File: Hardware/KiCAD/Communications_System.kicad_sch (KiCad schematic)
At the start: 1 part, among them IC2 CC1200RHBR

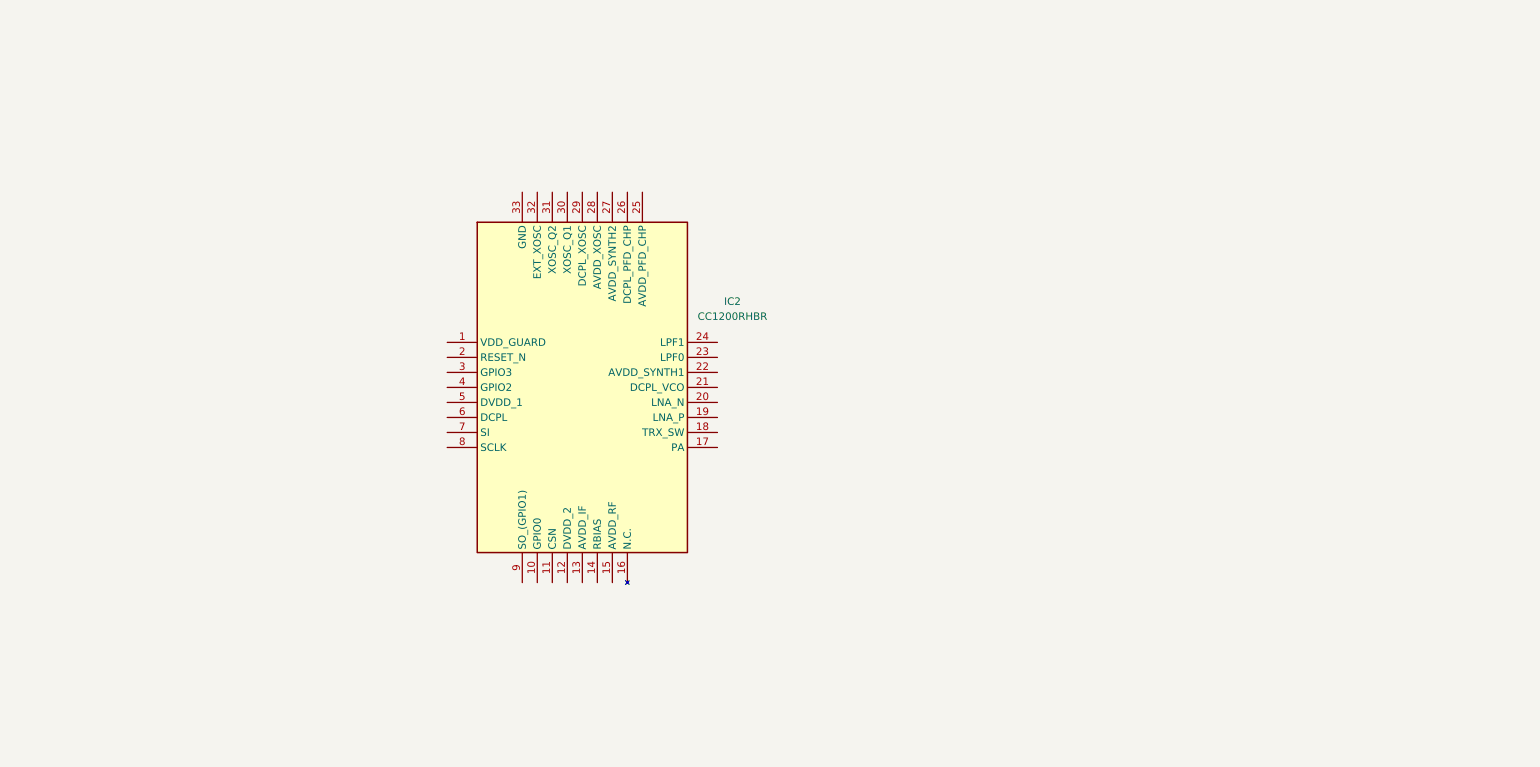
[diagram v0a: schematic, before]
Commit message: feat: Connect ESP32 to CC1200
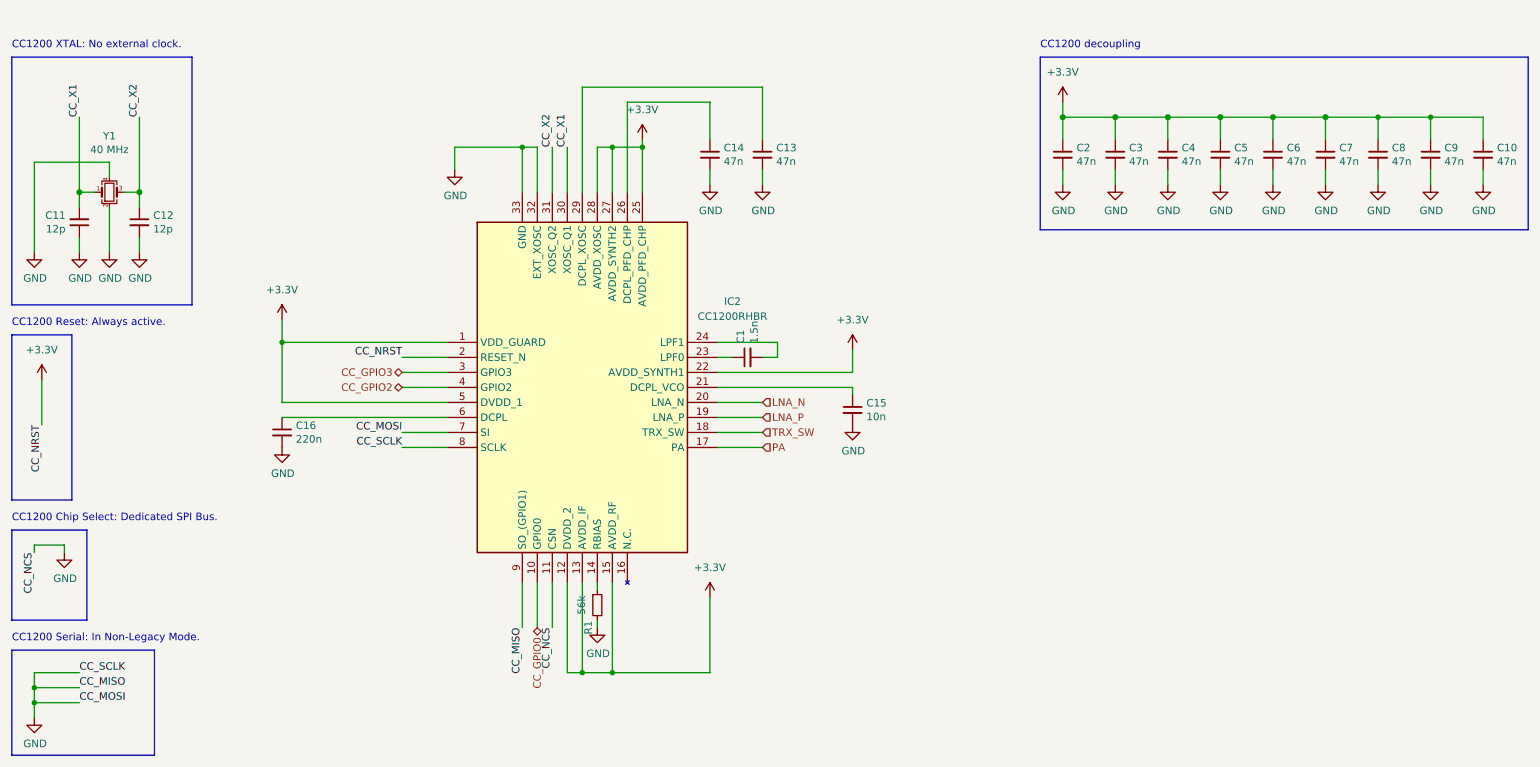
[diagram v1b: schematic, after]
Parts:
- added C1: 1.5n, Capacitor_SMD:C_0402_1005Metric, symbol pkl_device:pkl_C_Small
- added C10, C13, C14, C2, C3, C4, C5, C6, C7, C8, C9: 47n, Capacitor_SMD:C_0402_1005Metric, symbol pkl_device:pkl_C_Small
- added C11, C12: 12p, Capacitor_SMD:C_0402_1005Metric, symbol pkl_device:pkl_C_Small
- added C15: 10n, Capacitor_SMD:C_0402_1005Metric, symbol pkl_device:pkl_C_Small
- added C16: 220n, Capacitor_SMD:C_0402_1005Metric, symbol pkl_device:pkl_C_Small
- added R1: 56k, Resistor_SMD:R_0402_1005Metric, symbol pkl_device:pkl_R_Small
- added Y1: 40 MHz, Crystal:Crystal_SMD_3225-4Pin_3.2x2.5mm, symbol Device:Crystal_GND24_Small
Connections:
- net +3.3V: now reaches IC2.1 (VDD_GUARD)
- net +3.3V: now also IC2.12 (DVDD_2), IC2.13 (AVDD_IF), IC2.15 (AVDD_RF), IC2.2 (RESET_N), IC2.22 (AVDD_SYNTH1), IC2.25 (AVDD_PFD_CHP), IC2.27 (AVDD_SYNTH2), IC2.28 (AVDD_XOSC), IC2.5 (DVDD_1), C10.1, C2.1, C3.1, C4.1, C5.1, C6.1, C7.1, C8.1, C9.1
- net CC_GPIO0: now reaches IC2.10 (GPIO0)
- net GND: now reaches IC2.11 (CSN)
- net GND: now also IC2.32 (EXT_XOSC), IC2.33 (GND), IC2.7 (SI), IC2.8 (SCLK), IC2.9 (SO_(GPIO1)), C10.2, C11.1, C12.2, C13.2, C14.2, C15.2, C16.2, C2.2, C3.2, C4.2, C5.2, C6.2, C7.2, C8.2, C9.2, R1.2, Y1.2, Y1.4
- net at IC2.14 (RBIAS): now also R1.1
- net PA: now reaches IC2.17 (PA)
- net TRX_SW: now reaches IC2.18 (TRX_SW)
- net LNA_P: now reaches IC2.19 (LNA_P)
- net LNA_N: now reaches IC2.20 (LNA_N)
- net at IC2.21 (DCPL_VCO): now also C15.1
- net at IC2.23 (LPF0): now also C1.1
- net at IC2.24 (LPF1): now also C1.2
- net at IC2.26 (DCPL_PFD_CHP): now also C14.1
- net at IC2.29 (DCPL_XOSC): now also C13.1
- net CC_GPIO3: now reaches IC2.3 (GPIO3)
- net CC_X1: now reaches IC2.30 (XOSC_Q1)
- net CC_X1: now also C11.2, Y1.1
- net CC_X2: now reaches IC2.31 (XOSC_Q2)
- net CC_X2: now also C12.1, Y1.3
- net CC_GPIO2: now reaches IC2.4 (GPIO2)
- net at IC2.6 (DCPL): now also C16.1
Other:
- note added: "CC1200 Chip Select: Dedicated SPI Bus."
- note added: "CC1200 Reset: Always active."
- note added: "CC1200 Serial: In Non-Legacy Mode."
- note added: "CC1200 XTAL: No external clock."
- note added: "CC1200 decoupling"
- title: (none) -> RF Communications System

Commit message: feat: add models, correct hierarchical patterns
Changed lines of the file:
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@@
     (effects (font (size 1.27 1.27)) (justify left bottom))
-  )
-  (label "CC_MOSI" (at 85.09 83.82 180) (fields_autoplaced)
-    (effects (font (size 1.27 1.27)) (justify right bottom))
   )
   (label "CC_X1" (at 113.03 35.56 90) (fields_autoplaced)
@@
     (effects (font (size 1.27 1.27)) (justify left bottom))
   )
-  (label "CC_MISO" (at 105.41 116.84 270) (fields_autoplaced)
-    (effects (font (size 1.27 1.27)) (justify right bottom))
+  (label "CC_X2" (at 219.71 73.66 90) (fields_autoplaced)
+    (effects (font (size 1.27 1.27)) (justify left bottom))
   )
   (label "CC_NCS" (at 22.86 104.14 270) (fields_autoplaced)
     (effects (font (size 1.27 1.27)) (justify right bottom))
   )
+  (label "CC_X1" (at 209.55 73.66 90) (fields_autoplaced)
+    (effects (font (size 1.27 1.27)) (justify left bottom))
+  )
   (label "CC_X2" (at 110.49 35.56 90) (fields_autoplaced)
     (effects (font (size 1.27 1.27)) (justify left bottom))
   )
-  (label "CC_SCLK" (at 85.09 86.36 180) (fields_autoplaced)
-    (effects (font (size 1.27 1.27)) (justify right bottom))
-  )
-  (label "CC_NCS" (at 110.49 116.84 270) (fields_autoplaced)
-    (effects (font (size 1.27 1.27)) (justify right bottom))
-  )
   (label "CC_NRST" (at 24.13 82.55 270) (fields_autoplaced)
     (effects (font (size 1.27 1.27)) (justify right bottom))
@@
     (effects (font (size 1.27 1.27)) (justify left bottom))
   )
+  (hierarchical_label "CC_NCS" (shape input) (at 110.49 116.84 270) (fields_autoplaced)
+    (effects (font (size 1.27 1.27)) (justify right))
+  )
   (hierarchical_label "CC_GPIO3" (shape bidirectional) (at 85.09 73.66 180) (fields_autoplaced)
     (effects (font (size 1.27 1.27)) (justify right))
@@
     (effects (font (size 1.27 1.27)) (justify left))
   )
+  (hierarchical_label "CC_MISO" (shape output) (at 105.41 116.84 270) (fields_autoplaced)
+    (effects (font (size 1.27 1.27)) (justify right))
+  )
   (hierarchical_label "LNA_P" (shape input) (at 146.05 81.28 0) (fields_autoplaced)
     (effects (font (size 1.27 1.27)) (justify left))
   )
+  (hierarchical_label "CC_MOSI" (shape input) (at 85.09 83.82 180) (fields_autoplaced)
+    (effects (font (size 1.27 1.27)) (justify right))
+  )
   (hierarchical_label "PA" (shape input) (at 146.05 86.36 0) (fields_autoplaced)
     (effects (font (size 1.27 1.27)) (justify left))
@@
   (hierarchical_label "LNA_N" (shape input) (at 146.05 78.74 0) (fields_autoplaced)
     (effects (font (size 1.27 1.27)) (justify left))
+  )
+  (hierarchical_label "CC_SCLK" (shape input) (at 85.09 86.36 180) (fields_autoplaced)
+    (effects (font (size 1.27 1.27)) (justify right))
   )
   (hierarchical_label "CC_GPIO2" (shape bidirectional) (at 85.09 76.2 180) (fields_autoplaced)
@@
         )
       )
+    )
+  )
+  (symbol (lib_id "power:GND") (at 204.47 88.9 0) (unit 1)
+    (in_bom yes) (on_board yes) (dnp no)
+    (property "Reference" "#PWR039" (at 204.47 95.25 0)
+      (effects (font (size 1.27 1.27)) hide)
+    )
+    (property "Value" "GND" (at 204.597 93.2942 0)
+      (effects (font (size 1.27 1.27)))
+    )
+    (property "Footprint" "" (at 204.47 88.9 0)
+      (effects (font (size 1.27 1.27)) hide)
+    )
+    (property "Datasheet" "" (at 204.47 88.9 0)
+      (effects (font (size 1.27 1.27)) hide)
+    )
+    (pin "1")
+    (instances
+      (project "Cobalt-Cowboy"
+        (path "/60a68eb1-aa0f-414e-b03b-965ad6b52dab/d80d452c-0cd9-4253-b692-c2cdb4b1394b"
+          (reference "#PWR039") (unit 1)
+        )
+      )
+      (project "Mini17"
+        (path "/c89c6552-5574-4959-bcaf-f05dfde21961/f4521ef1-9a41-474d-b880-30e1e54c8ecb"
+          (reference "#PWR039") (unit 1)
+        )
+      )

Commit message: added battery to start power systen
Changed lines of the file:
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@@
-    (effects (font (size 1.27 1.27)) (justify left bottom))
-  )
-  (label "CC_X2" (at 219.71 73.66 90) (fields_autoplaced)
     (effects (font (size 1.27 1.27)) (justify left bottom))
   )
   (label "CC_NCS" (at 22.86 104.14 270) (fields_autoplaced)
     (effects (font (size 1.27 1.27)) (justify right bottom))
-  )
-  (label "CC_X1" (at 209.55 73.66 90) (fields_autoplaced)
-    (effects (font (size 1.27 1.27)) (justify left bottom))
   )
   (label "CC_X2" (at 110.49 35.56 90) (fields_autoplaced)
@@
         )
       )
-    )
-  )
-  (symbol (lib_id "power:GND") (at 204.47 88.9 0) (unit 1)
-    (in_bom yes) (on_board yes) (dnp no)
-    (property "Reference" "#PWR039" (at 204.47 95.25 0)
-      (effects (font (size 1.27 1.27)) hide)
-    )
-    (property "Value" "GND" (at 204.597 93.2942 0)
-      (effects (font (size 1.27 1.27)))
-    )
-    (property "Footprint" "" (at 204.47 88.9 0)
-      (effects (font (size 1.27 1.27)) hide)
-    )
-    (property "Datasheet" "" (at 204.47 88.9 0)
-      (effects (font (size 1.27 1.27)) hide)
-    )
-    (pin "1")
-    (instances
-      (project "Cobalt-Cowboy"
-        (path "/60a68eb1-aa0f-414e-b03b-965ad6b52dab/d80d452c-0cd9-4253-b692-c2cdb4b1394b"
-          (reference "#PWR039") (unit 1)
-        )
-      )
-      (project "Mini17"
-        (path "/c89c6552-5574-4959-bcaf-f05dfde21961/f4521ef1-9a41-474d-b880-30e1e54c8ecb"
-          (reference "#PWR039") (unit 1)
-        )
-      )

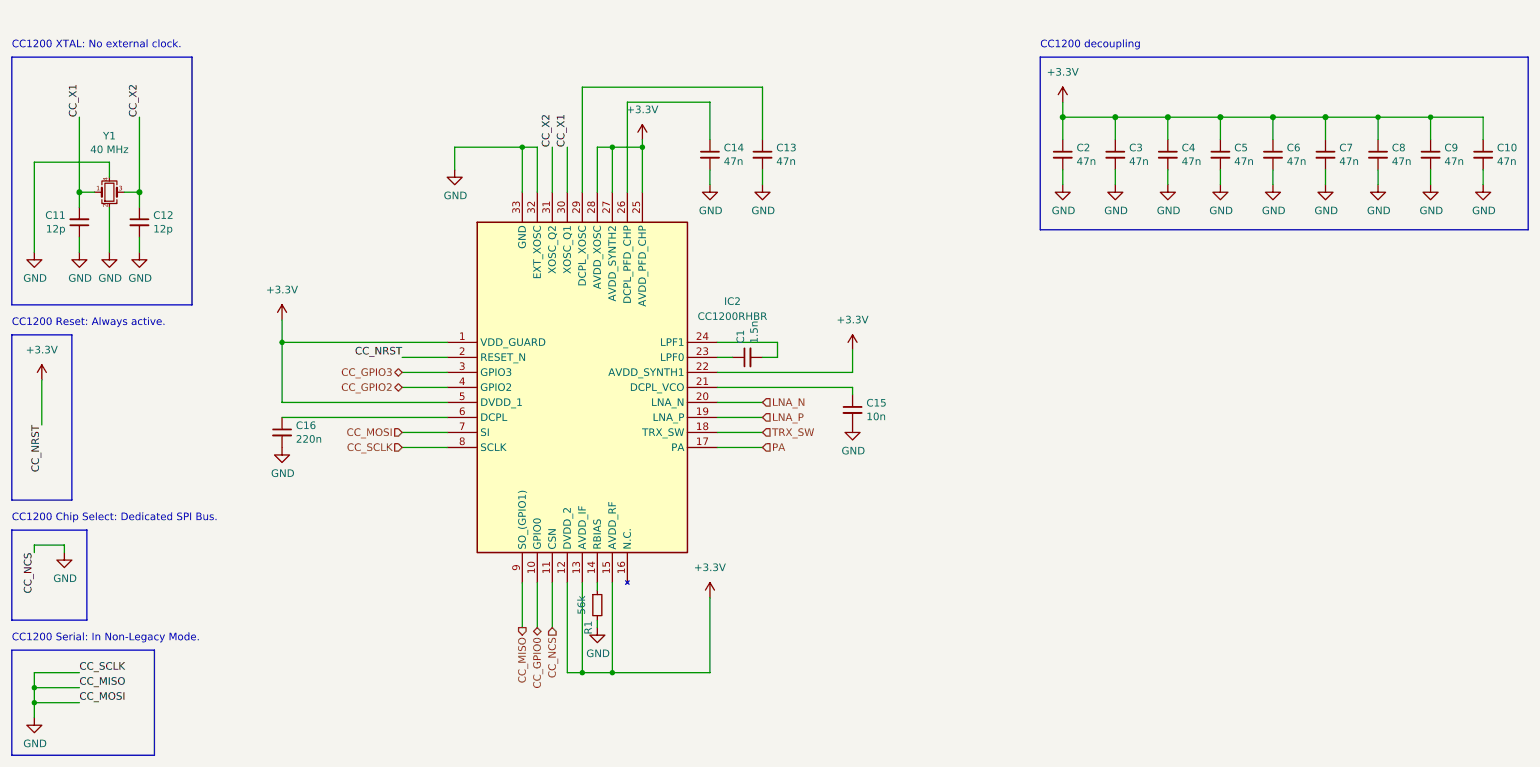
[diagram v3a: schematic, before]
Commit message: Renamed and added the kicad library
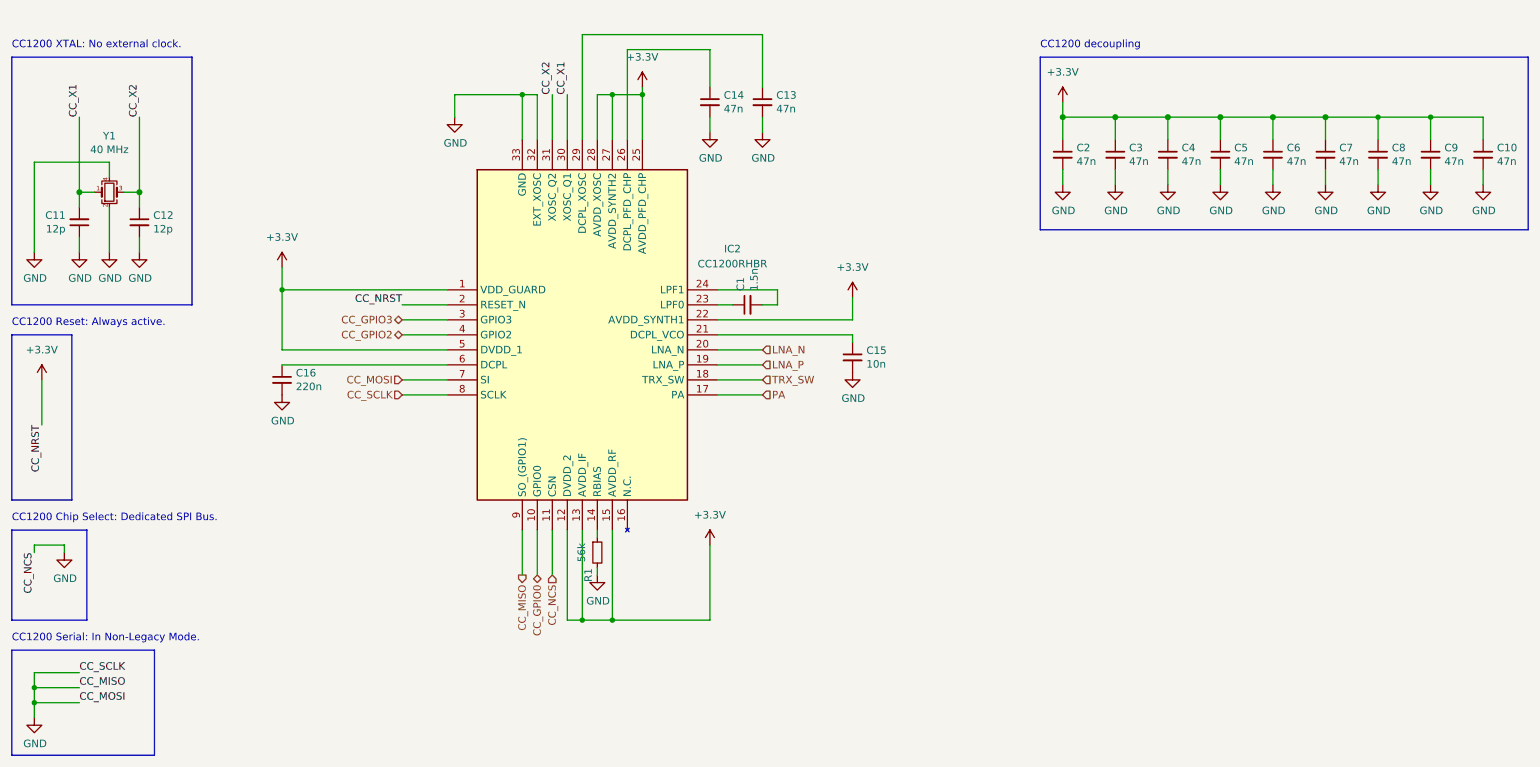
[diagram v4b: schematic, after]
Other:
- moved on the sheet: C1, C13, C14, C15, C16, IC2, R1
